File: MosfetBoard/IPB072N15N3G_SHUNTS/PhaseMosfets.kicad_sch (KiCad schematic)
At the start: 34 parts, among them J12 PHASE_PAD, Q1 IPB072N15N3G, Q2 IPB072N15N3G, Q4 IPB072N15N3G, Q5 IPB072N15N3G, U1 RS2166XC5, U4 NCS2003ASN2T1G

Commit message: ltc7801
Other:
- note added: "Total 0.00025Ω"
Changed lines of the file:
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@@
+    (effects (font (size 1.27 1.27)) (justify left bottom))
+  )
+  (text "Total 0.00025Ω" (at 63.5 139.7 0)
     (effects (font (size 1.27 1.27)) (justify left bottom))
   )

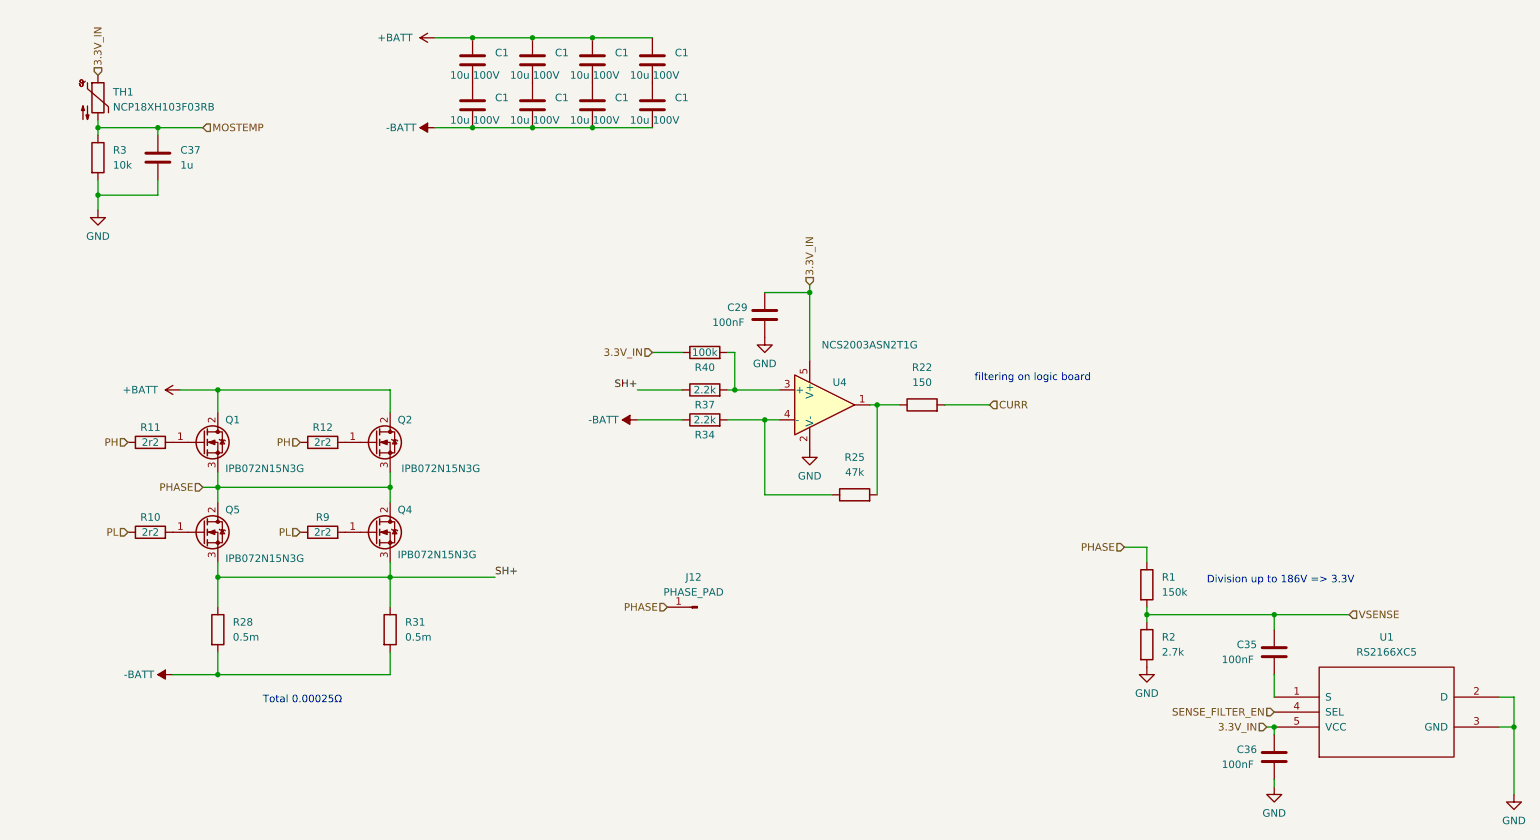
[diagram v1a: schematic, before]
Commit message: fixing_giga_mistake
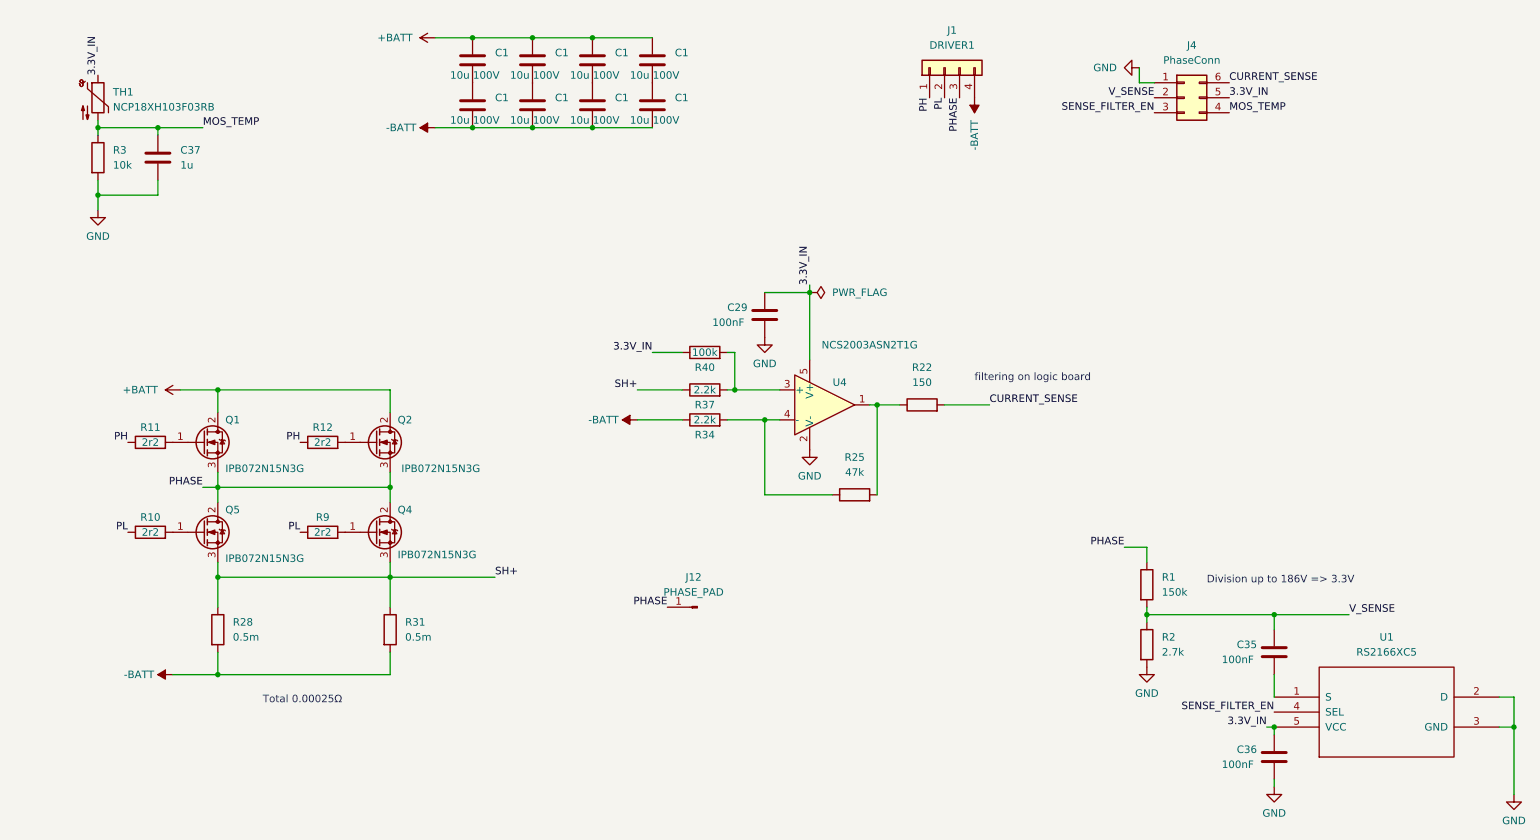
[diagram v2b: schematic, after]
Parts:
- added J1: DRIVER1, Connector_PinSocket_2.54mm:PinSocket_2x02_P2.54mm_Vertical_SMD, symbol Connector_Generic:Conn_01x04
- added J4: PhaseConn, Connector_PinSocket_2.54mm:PinSocket_2x03_P2.54mm_Vertical_SMD, symbol Connector_Generic:Conn_02x03_Counter_Clockwise
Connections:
- net -BATT: now also J1.4 (Pin_4)
- net 3.3V_IN: now also J4.5 (Pin_5)
- net GND: now also J4.1 (Pin_1)
- net PH: now also J1.1 (Pin_1)
- net PHASE: now also J1.3 (Pin_3)
- net PL: now also J1.2 (Pin_2)
- net SENSE_FILTER_EN: now also J4.3 (Pin_3)
- net CURR renamed CURRENT_SENSE
- net CURRENT_SENSE: now also J4.6 (Pin_6)
- net MOSTEMP renamed MOS_TEMP
- net MOS_TEMP: now also J4.4 (Pin_4)
- net VSENSE renamed V_SENSE
- net V_SENSE: now also J4.2 (Pin_2)

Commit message: cleanup
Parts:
- C1: MPN (none) -> C5156756
- C29, C36: footprint Capacitor_SMD:C_0805_2012Metric -> GigaVescLibs:C_0603_1608Metric_L; MPN C28233 -> C14663
- C35: footprint Capacitor_SMD:C_1206_3216Metric -> GigaVescLibs:C_0603_1608Metric_L; MPN C24497 -> C14663
- C37: footprint Capacitor_SMD:C_0805_2012Metric -> GigaVescLibs:C_0603_1608Metric_L; MPN C28323 -> C15849
- R1: footprint Resistor_SMD:R_0805_2012Metric -> Resistor_SMD:R_0603_1608Metric; MPN C17470 -> C22807
- R10, R11, R12, R9: value 2r2 -> 2.2; footprint Resistor_SMD:R_0805_2012Metric -> Resistor_SMD:R_0603_1608Metric; MPN C17521 -> C22939
- R2: footprint Resistor_SMD:R_0805_2012Metric -> Resistor_SMD:R_0603_1608Metric; MPN C17530 -> C13167
- R22: footprint Resistor_SMD:R_0805_2012Metric -> Resistor_SMD:R_0603_1608Metric; MPN C17471 -> C22808
- R25: footprint Resistor_SMD:R_0805_2012Metric -> Resistor_SMD:R_0603_1608Metric; MPN C17713 -> C25819
- R3: footprint Resistor_SMD:R_0805_2012Metric -> Resistor_SMD:R_0603_1608Metric; MPN C17414 -> C25804
- R34, R37: footprint Resistor_SMD:R_0805_2012Metric -> Resistor_SMD:R_0603_1608Metric; MPN C17520 -> C4190
- R40: footprint Resistor_SMD:R_0805_2012Metric -> Resistor_SMD:R_0603_1608Metric; MPN C149504 -> C25803
- U4: JLCRotOffset (none) -> -180
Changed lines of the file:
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@@
+      (effects (font (size 1.27 1.27)) hide)
+    )
+    (property "JLCRotOffset" "-180" (at 158.75 88.9 0)
       (effects (font (size 1.27 1.27)) hide)
     )
@@
       (effects (font (size 1.27 1.27)) hide)
     )
+    (property "MPN" "C5156756" (at 129.54 30.48 0)
+      (effects (font (size 1.27 1.27)) hide)
+    )
     (pin "1")
     (pin "2")
@@
       (effects (font (size 1.27 1.27)) (justify left))
     )
-    (property "Footprint" "Resistor_SMD:R_0805_2012Metric" (at 211.582 119.38 90)
+    (property "Footprint" "Resistor_SMD:R_0603_1608Metric" (at 211.582 119.38 90)
       (effects (font (size 1.27 1.27)) hide)
     )
@@
       (effects (font (size 1.27 1.27)) hide)
     )
-    (property "MPN" "C17470" (at 213.36 119.38 0)
+    (property "MPN" "C22807" (at 213.36 119.38 0)
       (effects (font (size 1.27 1.27)) hide)
     )
@@
       (effects (font (size 1.27 1.27)))
     )
-    (property "Footprint" "Resistor_SMD:R_0805_2012Metric" (at 138.43 88.138 90)
+    (property "Footprint" "Resistor_SMD:R_0603_1608Metric" (at 138.43 88.138 90)
       (effects (font (size 1.27 1.27)) hide)
     )
@@
       (effects (font (size 1.27 1.27)) hide)
     )
-    (property "MPN" "C17520" (at 138.43 86.36 0)
+    (property "MPN" "C4190" (at 138.43 86.36 0)
       (effects (font (size 1.27 1.27)) hide)
     )
@@
       (effects (font (size 1.27 1.27)) hide)
     )
+    (property "MPN" "C5156756" (at 129.54 38.1 0)
+      (effects (font (size 1.27 1.27)) hide)
+    )
     (pin "1")
     (pin "2")
@@
       (effects (font (size 1.27 1.27)) hide)
     )
+    (property "MPN" "C5156756" (at 109.22 38.1 0)
+      (effects (font (size 1.27 1.27)) hide)
+    )
     (pin "1")
     (pin "2")
@@
       (effects (font (size 1.27 1.27)) (justify left))
     )
-    (property "Footprint" "Capacitor_SMD:C_1206_3216Metric" (at 235.9152 134.62 0)
+    (property "Footprint" "GigaVescLibs:C_0603_1608Metric_L" (at 235.9152 134.62 0)
       (effects (font (size 1.27 1.27)) hide)
     )
@@
       (effects (font (size 1.27 1.27)) hide)
     )
-    (property "MPN" "C24497" (at 234.95 130.81 0)
+    (property "MPN" "C14663" (at 234.95 130.81 0)
       (effects (font (size 1.27 1.27)) hide)
     )
@@
       (effects (font (size 1.27 1.27)))
     )
-    (property "Value" "2r2" (at 73.66 95.25 90)
-      (effects (font (size 1.27 1.27)))
-    )
-    (property "Footprint" "Resistor_SMD:R_0805_2012Metric" (at 73.66 97.028 90)
+    (property "Value" "2.2" (at 73.66 95.25 90)
+      (effects (font (size 1.27 1.27)))
+    )
+    (property "Footprint" "Resistor_SMD:R_0603_1608Metric" (at 73.66 97.028 90)
       (effects (font (size 1.27 1.27)) hide)
     )
@@
       (effects (font (size 1.27 1.27)) hide)
     )
-    (property "MPN" "C17521" (at 73.66 95.25 90)
+    (property "MPN" "C22939" (at 73.66 95.25 90)
       (effects (font (size 1.27 1.27)) hide)
     )
@@
       (effects (font (size 1.27 1.27)))
     )
-    (property "Value" "2r2" (at 44.45 95.25 90)
-      (effects (font (size 1.27 1.27)))
-    )
-    (property "Footprint" "Resistor_SMD:R_0805_2012Metric" (at 44.45 97.028 90)
+    (property "Value" "2.2" (at 44.45 95.25 90)
+      (effects (font (size 1.27 1.27)))
+    )
+    (property "Footprint" "Resistor_SMD:R_0603_1608Metric" (at 44.45 97.028 90)
       (effects (font (size 1.27 1.27)) hide)
     )
@@
       (effects (font (size 1.27 1.27)) hide)
     )
-    (property "MPN" "C17521" (at 44.45 95.25 90)
+    (property "MPN" "C22939" (at 44.45 95.25 90)
       (effects (font (size 1.27 1.27)) hide)
     )
@@
       (effects (font (size 1.27 1.27)) (justify left))
     )
-    (property "Footprint" "Resistor_SMD:R_0805_2012Metric" (at 33.782 46.99 90)
+    (property "Footprint" "Resistor_SMD:R_0603_1608Metric" (at 33.782 46.99 90)
       (effects (font (size 1.27 1.27)) hide)
     )
@@
       (effects (font (size 1.27 1.27)) hide)
     )
-    (property "MPN" "C17414" (at 35.56 46.99 0)
+    (property "MPN" "C25804" (at 35.56 46.99 0)
       (effects (font (size 1.27 1.27)) hide)
     )
@@
       (effects (font (size 1.27 1.27)) (justify left))
     )
-    (property "Footprint" "Capacitor_SMD:C_0805_2012Metric" (at 46.6852 50.8 0)
+    (property "Footprint" "GigaVescLibs:C_0603_1608Metric_L" (at 46.6852 50.8 0)
       (effects (font (size 1.27 1.27)) hide)
     )
@@
       (effects (font (size 1.27 1.27)) hide)
     )
-    (property "MPN" "C28323" (at 45.72 46.99 0)
+    (property "MPN" "C15849" (at 45.72 46.99 0)
       (effects (font (size 1.27 1.27)) hide)
     )
@@
       (effects (font (size 1.27 1.27)))
     )
-    (property "Value" "2r2" (at 44.45 110.49 90)
-      (effects (font (size 1.27 1.27)))
-    )
-    (property "Footprint" "Resistor_SMD:R_0805_2012Metric" (at 44.45 112.268 90)
+    (property "Value" "2.2" (at 44.45 110.49 90)
+      (effects (font (size 1.27 1.27)))
+    )
+    (property "Footprint" "Resistor_SMD:R_0603_1608Metric" (at 44.45 112.268 90)
       (effects (font (size 1.27 1.27)) hide)
     )
@@
       (effects (font (size 1.27 1.27)) hide)
     )
-    (property "MPN" "C17521" (at 44.45 110.49 90)
+    (property "MPN" "C22939" (at 44.45 110.49 90)
       (effects (font (size 1.27 1.27)) hide)
     )
@@
       (effects (font (size 1.27 1.27)))
     )
-    (property "Footprint" "Resistor_SMD:R_0805_2012Metric" (at 163.83 105.918 90)
+    (property "Footprint" "Resistor_SMD:R_0603_1608Metric" (at 163.83 105.918 90)
       (effects (font (size 1.27 1.27)) hide)
     )
@@
       (effects (font (size 1.27 1.27)) hide)
     )
-    (property "MPN" "C17713" (at 163.83 104.14 0)
+    (property "MPN" "C25819" (at 163.83 104.14 0)
       (effects (font (size 1.27 1.27)) hide)
     )
@@
       (effects (font (size 1.27 1.27)))
     )
-    (property "Value" "2r2" (at 73.66 110.49 90)
-      (effects (font (size 1.27 1.27)))
-    )
-    (property "Footprint" "Resistor_SMD:R_0805_2012Metric" (at 73.66 112.268 90)
+    (property "Value" "2.2" (at 73.66 110.49 90)
+      (effects (font (size 1.27 1.27)))
+    )
+    (property "Footprint" "Resistor_SMD:R_0603_1608Metric" (at 73.66 112.268 90)
       (effects (font (size 1.27 1.27)) hide)
     )
@@
       (effects (font (size 1.27 1.27)) hide)
     )
-    (property "MPN" "C17521" (at 73.66 110.49 90)
+    (property "MPN" "C22939" (at 73.66 110.49 90)
       (effects (font (size 1.27 1.27)) hide)
     )
@@
       (effects (font (size 1.27 1.27)))
     )
-    (property "Footprint" "Resistor_SMD:R_0805_2012Metric" (at 175.26 90.678 90)
+    (property "Footprint" "Resistor_SMD:R_0603_1608Metric" (at 175.26 90.678 90)
       (effects (font (size 1.27 1.27)) hide)
     )
@@
       (effects (font (size 1.27 1.27)) hide)
     )
-    (property "MPN" "C17471" (at 175.26 88.9 0)
+    (property "MPN" "C22808" (at 175.26 88.9 0)
       (effects (font (size 1.27 1.27)) hide)
     )
@@
       (effects (font (size 1.27 1.27)))
     )
-    (property "Footprint" "Resistor_SMD:R_0805_2012Metric" (at 138.43 81.788 90)
+    (property "Footprint" "Resistor_SMD:R_0603_1608Metric" (at 138.43 81.788 90)
       (effects (font (size 1.27 1.27)) hide)
     )
@@
       (effects (font (size 1.27 1.27)) hide)
     )
-    (property "MPN" "C149504" (at 138.43 80.01 0)
+    (property "MPN" "C25803" (at 138.43 80.01 0)
       (effects (font (size 1.27 1.27)) hide)
     )
@@
       (effects (font (size 1.27 1.27)) (justify left))
     )
-    (property "Footprint" "Capacitor_SMD:C_0805_2012Metric" (at 149.5552 77.47 0)
+    (property "Footprint" "GigaVescLibs:C_0603_1608Metric_L" (at 149.5552 77.47 0)
       (effects (font (size 1.27 1.27)) hide)
     )
@@
       (effects (font (size 1.27 1.27)) hide)
     )
-    (property "MPN" "C28233" (at 148.59 73.66 0)
+    (property "MPN" "C14663" (at 148.59 73.66 0)
       (effects (font (size 1.27 1.27)) hide)
     )
@@
       (effects (font (size 1.27 1.27)) (justify left))
     )
-    (property "Footprint" "Resistor_SMD:R_0805_2012Metric" (at 211.582 129.54 90)
+    (property "Footprint" "Resistor_SMD:R_0603_1608Metric" (at 211.582 129.54 90)
       (effects (font (size 1.27 1.27)) hide)
     )
@@
       (effects (font (size 1.27 1.27)) hide)
     )
-    (property "MPN" "C17530" (at 213.36 129.54 0)
+    (property "MPN" "C13167" (at 213.36 129.54 0)
       (effects (font (size 1.27 1.27)) hide)
     )
@@
       (effects (font (size 1.27 1.27)) hide)
     )
+    (property "MPN" "C5156756" (at 109.22 30.48 0)
+      (effects (font (size 1.27 1.27)) hide)
+    )
     (pin "1")
     (pin "2")
@@
       (effects (font (size 1.27 1.27)) hide)
     )
+    (property "MPN" "C5156756" (at 119.38 30.48 0)
+      (effects (font (size 1.27 1.27)) hide)
+    )
     (pin "1")
     (pin "2")
@@
       (effects (font (size 1.27 1.27)) (justify left))
     )
-    (property "Footprint" "Capacitor_SMD:C_0805_2012Metric" (at 235.9152 152.4 0)
+    (property "Footprint" "GigaVescLibs:C_0603_1608Metric_L" (at 235.9152 152.4 0)
       (effects (font (size 1.27 1.27)) hide)
     )
@@
       (effects (font (size 1.27 1.27)) hide)
     )
-    (property "MPN" "C28233" (at 234.95 148.59 0)
+    (property "MPN" "C14663" (at 234.95 148.59 0)
       (effects (font (size 1.27 1.27)) hide)
     )
@@
       (effects (font (size 1.27 1.27)))
     )
-    (property "Footprint" "Resistor_SMD:R_0805_2012Metric" (at 138.43 93.218 90)
+    (property "Footprint" "Resistor_SMD:R_0603_1608Metric" (at 138.43 93.218 90)
       (effects (font (size 1.27 1.27)) hide)
     )
@@
       (effects (font (size 1.27 1.27)) hide)
     )
-    (property "MPN" "C17520" (at 138.43 91.44 0)
+    (property "MPN" "C4190" (at 138.43 91.44 0)
       (effects (font (size 1.27 1.27)) hide)
     )
@@
       (effects (font (size 1.27 1.27)) hide)
     )
+    (property "MPN" "C5156756" (at 119.38 38.1 0)
+      (effects (font (size 1.27 1.27)) hide)
+    )
     (pin "1")
     (pin "2")
@@
       (effects (font (size 1.27 1.27)) hide)
     )
+    (property "MPN" "C5156756" (at 99.06 38.1 0)
+      (effects (font (size 1.27 1.27)) hide)
+    )

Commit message: v2.3
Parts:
- removed C35, C36: 100nF, GigaVescLibs:C_0603_1608Metric_L, symbol Device:C
- removed U1: RS2166XC5, Package_TO_SOT_SMD:SOT-353_SC-70-5, symbol GigaESCSymbols:RS2166XC5
- added JP1: DummyJumper, symbol Jumper:Jumper_2_Bridged
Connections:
- net -BATT: now also JP1.1 (A)
- net SENSE_FILTER_EN: no longer names the net of J4.3 (Pin_3)
- new net SH-: JP1.2 (B)
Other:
- moved on the sheet: C29, J12, R1, R2, R22, R25, R34, R37, R40, U4

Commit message: small changes
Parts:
- removed C29: 100nF, GigaVescLibs:C_0603_1608Metric_L, symbol Device:C
- removed R22: 150, Resistor_SMD:R_0603_1608Metric, symbol Device:R
- removed R25: 47k, Resistor_SMD:R_0603_1608Metric, symbol Device:R
- removed R34, R37: 2.2k, Resistor_SMD:R_0603_1608Metric, symbol Device:R
- removed R40: 100k, Resistor_SMD:R_0603_1608Metric, symbol Device:R
- removed U4: NCS2003ASN2T1G, Package_SO:TSOP-5_1.65x3.05mm_P0.95mm, symbol Amplifier_Operational:NCS20071SN
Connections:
- net CURRENT_SENSE is gone; now on net SH+: J4.6 (Pin_6)
- net SH-: now also J4.3 (Pin_3)
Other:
- note removed: "filtering on logic board"

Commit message: v2.6.0 - cleanup
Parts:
- removed J12: PHASE_PAD, Connector_Wire:SolderWirePad_1x01_SMD_5x10mm, symbol Connector:Conn_01x01_Pin
- JP1: footprint (none) -> GigaVescLibs:SolderJumper0.3mm
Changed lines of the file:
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@@
-    (stroke (width 0) (type default))
-  )
-  (wire (pts (xy 85.09 102.87) (xy 106.68 102.87))
     (stroke (width 0) (type default))
   )
@@
       (effects (font (size 1.27 1.27)))
     )
-    (property "Footprint" "" (at 95.25 134.62 0)
+    (property "Footprint" "GigaVescLibs:SolderJumper0.3mm" (at 95.25 134.62 0)
       (effects (font (size 1.27 1.27)) hide)
     )
@@
         )
       )
-    )
-  )
-  (symbol (lib_id "Connector:Conn_01x01_Pin") (at 111.76 102.87 180) (unit 1)
-    (in_bom yes) (on_board yes) (dnp no) (fields_autoplaced)
-    (property "Reference" "J12" (at 111.125 97.79 0)
-      (effects (font (size 1.27 1.27)))
-    )
-    (property "Value" "PHASE_PAD" (at 111.125 100.33 0)
-      (effects (font (size 1.27 1.27)))
-    )
-    (property "Footprint" "Connector_Wire:SolderWirePad_1x01_SMD_5x10mm" (at 111.76 102.87 0)
-      (effects (font (size 1.27 1.27)) hide)
-    )
-    (property "Datasheet" "~" (at 111.76 102.87 0)
-      (effects (font (size 1.27 1.27)) hide)
-    )
-    (pin "1")
-    (instances
-      (project "IPB072N15N3G_SHUNTS"
-        (path "/8a7bb686-c87a-43a6-b3d4-d988e8a2213f"
-          (reference "J12") (unit 1)
-        )
-        (path "/8a7bb686-c87a-43a6-b3d4-d988e8a2213f/3d569e84-87d6-4696-b0ce-a4e576394c1a"
-          (reference "J7") (unit 1)
-        )
-        (path "/8a7bb686-c87a-43a6-b3d4-d988e8a2213f/db7451b3-bde8-4d72-ba04-6d13b057caad"
-          (reference "J15") (unit 1)
-        )
-        (path "/8a7bb686-c87a-43a6-b3d4-d988e8a2213f/ccaed507-63cb-4563-a707-3e0cba7d2643"
-          (reference "J16") (unit 1)
-        )
-      )
